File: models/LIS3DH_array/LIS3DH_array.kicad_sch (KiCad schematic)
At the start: 3 parts, among them J10 Conn_01x09_Socket, J11 Conn_01x03_Socket, J12 Conn_01x02_Socket

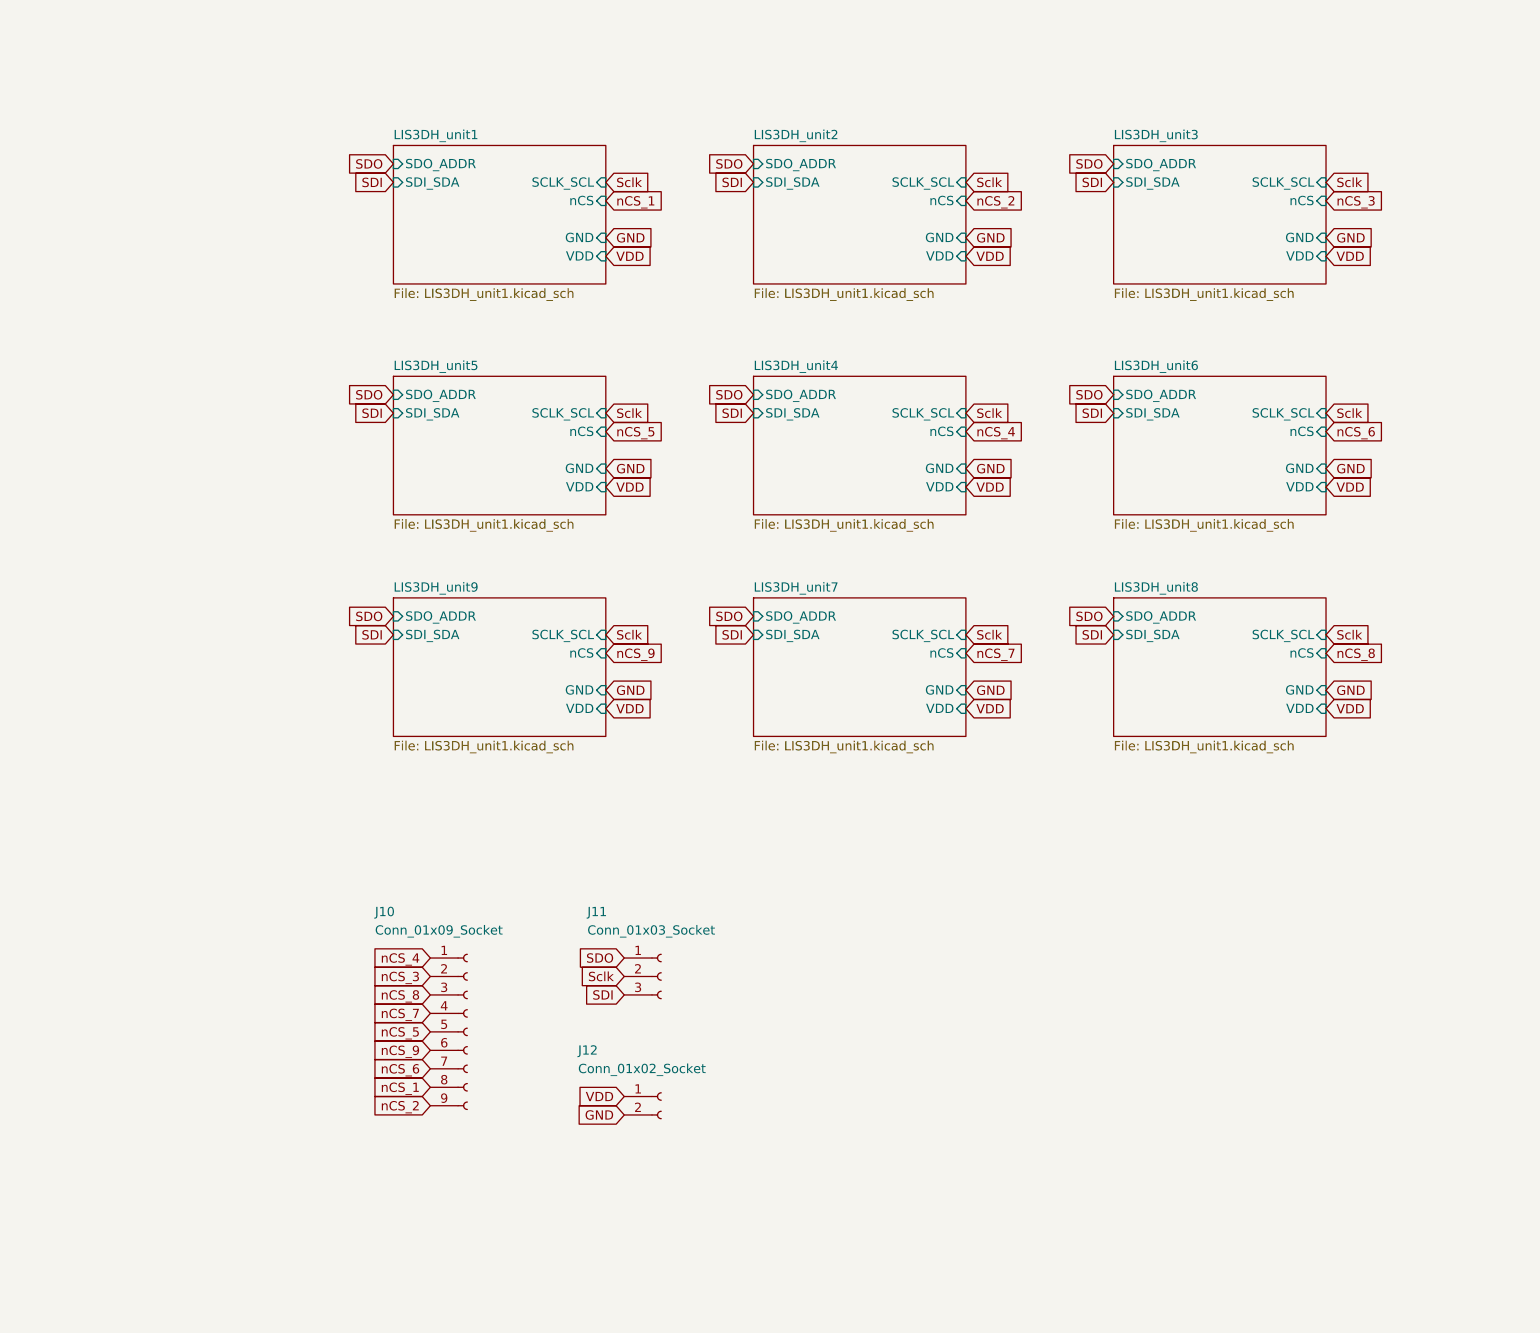
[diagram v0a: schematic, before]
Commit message: updated LIS3DH array
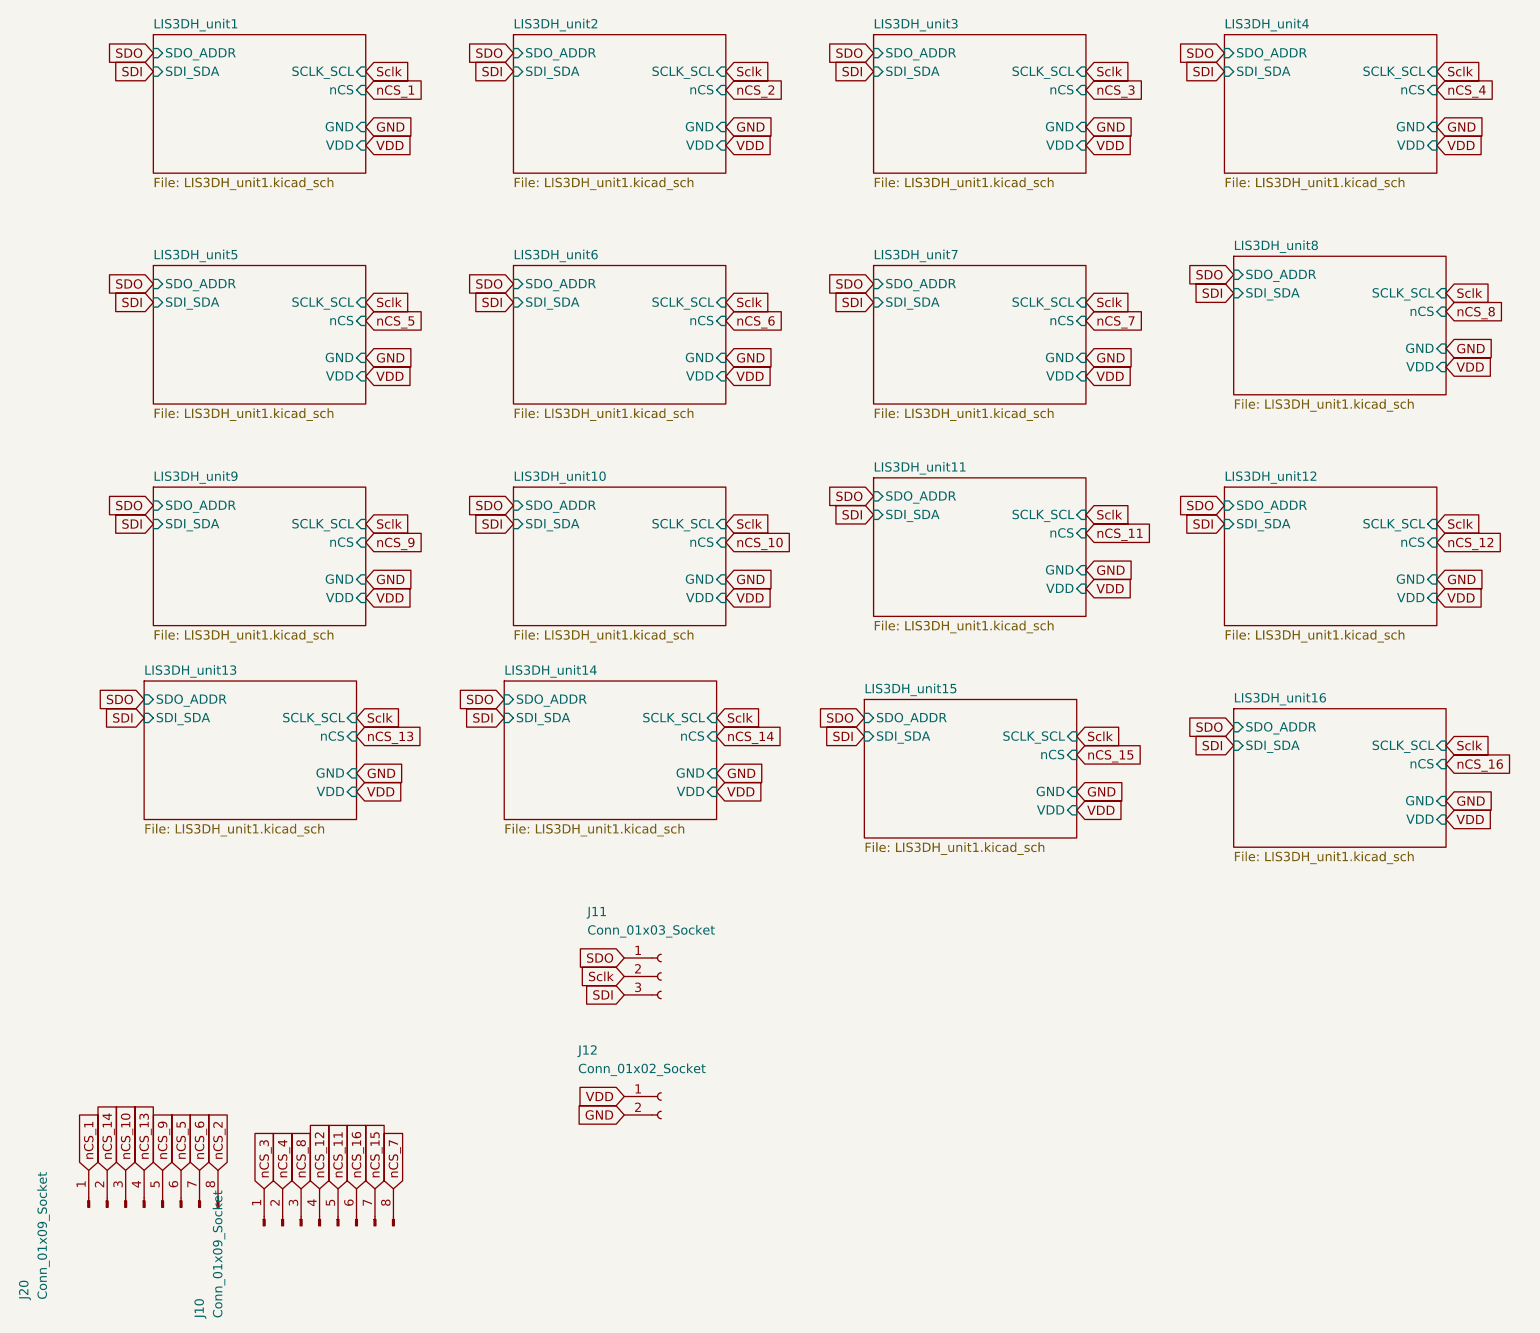
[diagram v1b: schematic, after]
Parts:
- added J20: Conn_01x09_Socket, Connector_PinHeader_2.54mm:PinHeader_1x08_P2.54mm_Vertical, symbol Connector:Conn_01x08_Pin
- J10: footprint Connector_PinHeader_2.54mm:PinHeader_1x09_P2.54mm_Vertical -> Connector_PinHeader_2.54mm:PinHeader_1x08_P2.54mm_Vertical; symbol Connector:Conn_01x09_Socket -> Connector:Conn_01x08_Pin
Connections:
- net nCS_1: now also J20.1 (Pin_1); no longer J10.8 (Pin_8)
- net nCS_2: now also J20.8 (Pin_8); no longer J10.9 (Pin_9)
- net nCS_3: now also J10.1 (Pin_1); no longer J10.2 (Pin_2)
- net nCS_4: now also J10.2 (Pin_2); no longer J10.1 (Pin_1)
- net nCS_5: now also J20.6 (Pin_6); no longer J10.5 (Pin_5)
- net nCS_6: now also J20.7 (Pin_7); no longer J10.7 (Pin_7)
- net nCS_7: now also J10.8 (Pin_8); no longer J10.4 (Pin_4)
- net nCS_9: now also J20.5 (Pin_5); no longer J10.6 (Pin_6)
- new net nCS_10: J20.3 (Pin_3)
- new net nCS_11: J10.5 (Pin_5)
- new net nCS_12: J10.4 (Pin_4)
- new net nCS_13: J20.4 (Pin_4)
- new net nCS_14: J20.2 (Pin_2)
- new net nCS_15: J10.7 (Pin_7)
- new net nCS_16: J10.6 (Pin_6)
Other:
- added sheet LIS3DH_unit10 (LIS3DH_unit1.kicad_sch)
- added sheet LIS3DH_unit11 (LIS3DH_unit1.kicad_sch)
- added sheet LIS3DH_unit12 (LIS3DH_unit1.kicad_sch)
- added sheet LIS3DH_unit13 (LIS3DH_unit1.kicad_sch)
- added sheet LIS3DH_unit14 (LIS3DH_unit1.kicad_sch)
- added sheet LIS3DH_unit15 (LIS3DH_unit1.kicad_sch)
- added sheet LIS3DH_unit16 (LIS3DH_unit1.kicad_sch)

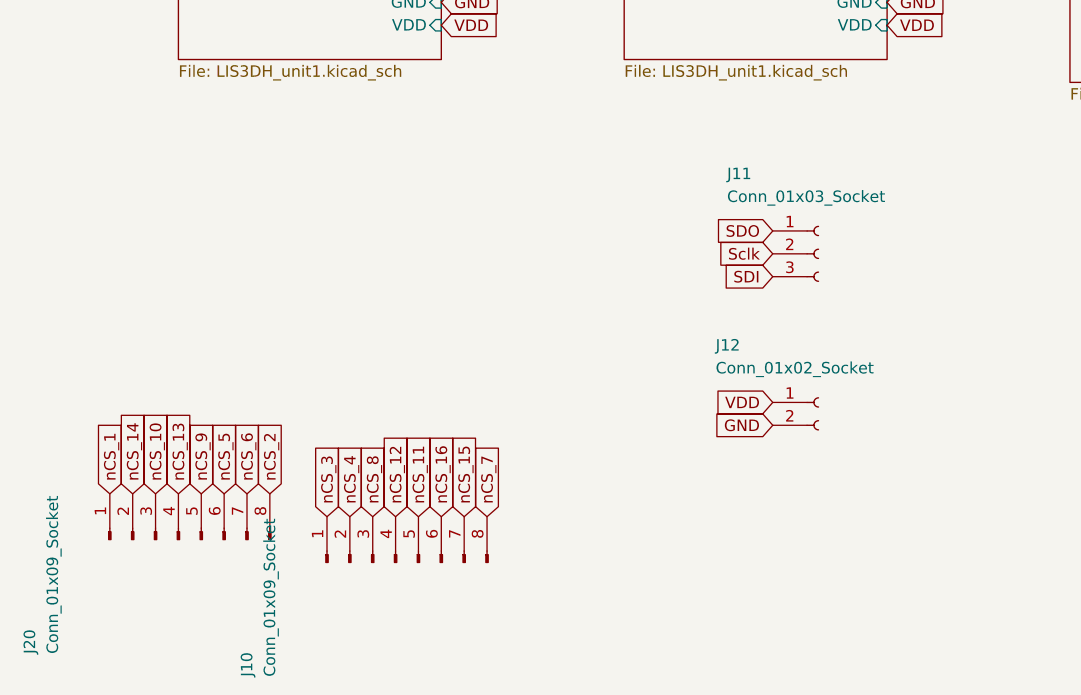
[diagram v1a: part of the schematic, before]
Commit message: updated lis3dh array: fpc connectors
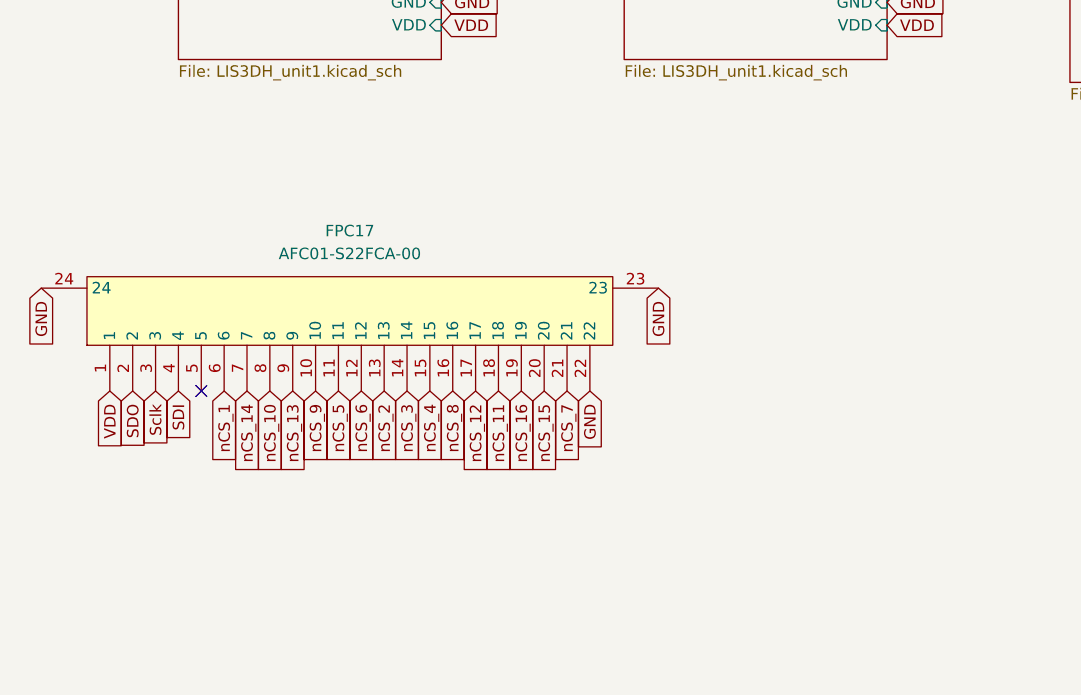
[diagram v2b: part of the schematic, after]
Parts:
- removed J10, J20: Conn_01x09_Socket, Connector_PinHeader_2.54mm:PinHeader_1x08_P2.54mm_Vertical, symbol Connector:Conn_01x08_Pin
- removed J11: Conn_01x03_Socket, Connector_PinHeader_2.54mm:PinHeader_1x03_P2.54mm_Vertical, symbol Connector:Conn_01x03_Socket
- removed J12: Conn_01x02_Socket, Connector_PinHeader_2.54mm:PinHeader_1x02_P2.54mm_Vertical, symbol Connector:Conn_01x02_Socket
- added FPC17: AFC01-S22FCA-00, 00_lcsc:FPC-SMD_P0.5-22P_FGS-XJ-H2.0, symbol 00_lcsc:AFC01-S22FCA-00
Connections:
- net GND: now also FPC17.22, FPC17.23, FPC17.24
- net SDI: now also FPC17.4
- net SDO: now also FPC17.2
- net Sclk: now also FPC17.3
- net VDD: now also FPC17.1
- net nCS_1: now also FPC17.6
- net nCS_10: now also FPC17.8
- net nCS_11: now also FPC17.18
- net nCS_12: now also FPC17.17
- net nCS_13: now also FPC17.9
- net nCS_14: now also FPC17.7
- net nCS_15: now also FPC17.20
- net nCS_16: now also FPC17.19
- net nCS_2: now also FPC17.13
- net nCS_3: now also FPC17.14
- net nCS_4: now also FPC17.15
- net nCS_5: now also FPC17.11
- net nCS_6: now also FPC17.12
- net nCS_7: now also FPC17.21
- net nCS_8: now also FPC17.16
- net nCS_9: now also FPC17.10
- no-connect marks 0 -> 1
